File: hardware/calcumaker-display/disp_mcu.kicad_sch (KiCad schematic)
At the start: 8 parts, among them J3 SWD TC2030-NL, U4 STM32G031K8U6

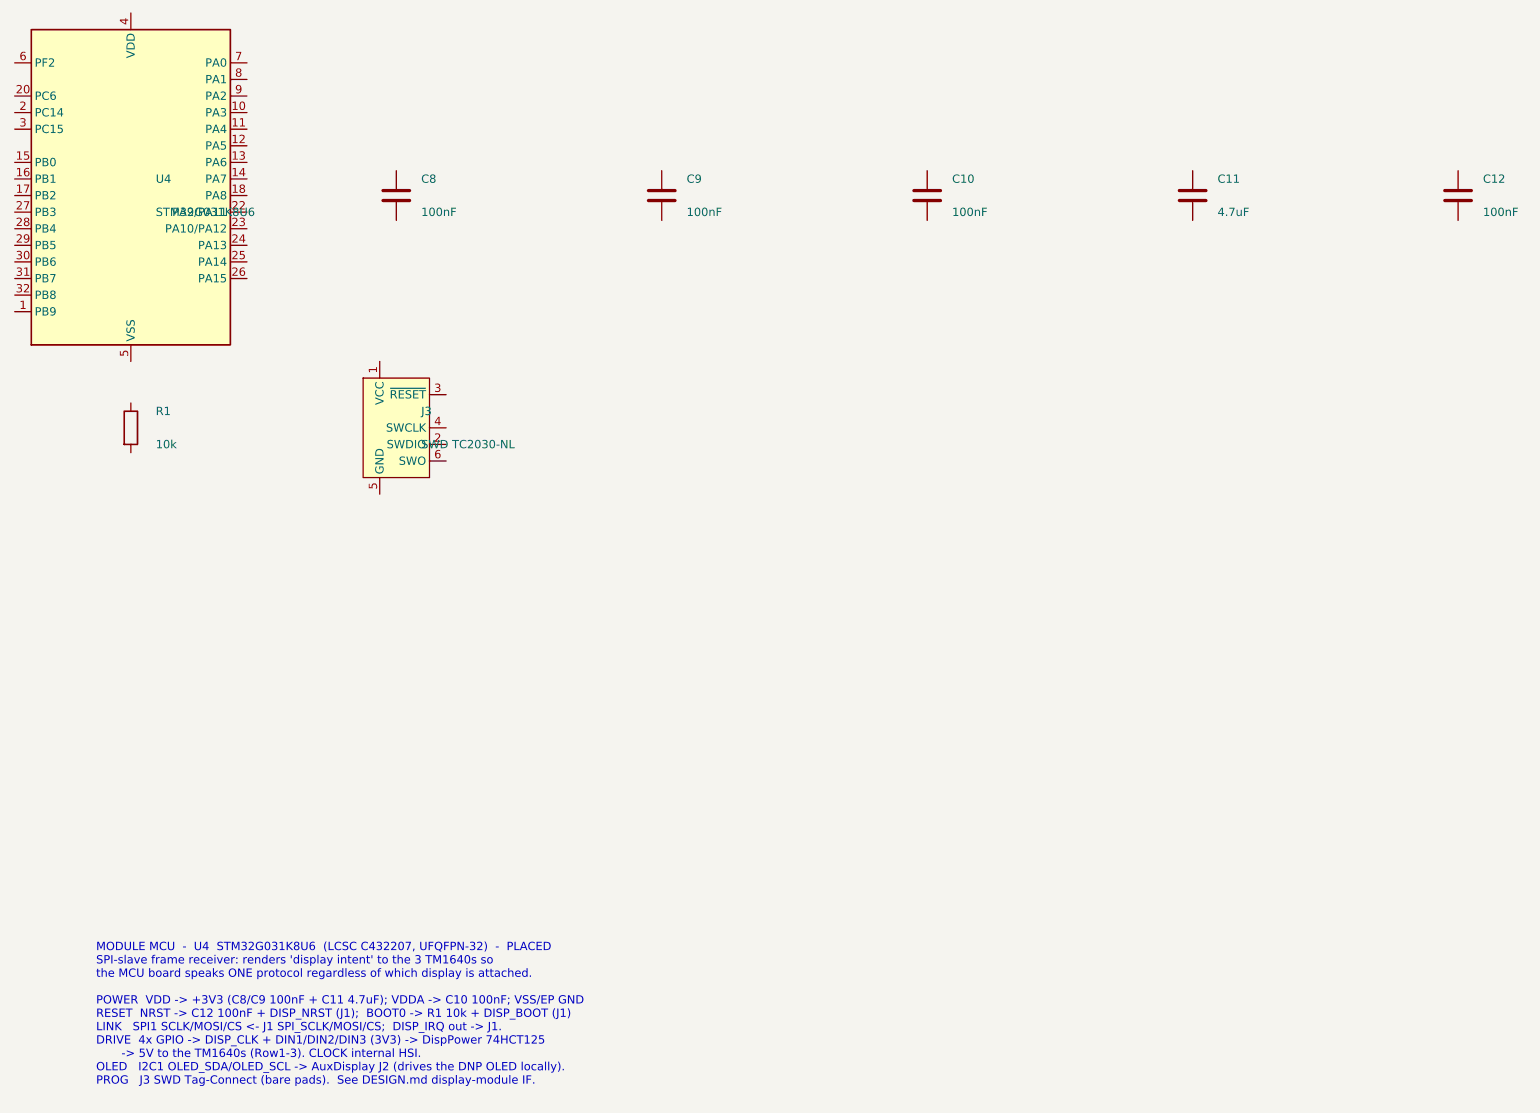
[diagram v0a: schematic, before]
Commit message: firmware: scaffold the two display-module targets + wire the module sheets
Firmware scaffold (all build; targets thumbv6m-none-eabi):
- calcumaker-display-proto: shared no_std wire protocol — the "display intent"
  DisplayFrame the U575 sends over SPI (text rows + flags + aux), with a
  fixed-length checksummed codec. Host-tested (cargo test: 3/3).
- calcumaker-display-fw: 7-seg module (STM32G031, embassy-stm32) — SPI-slave
  receiver + a bit-bang TM1640 driver + 7-seg render.
- calcumaker-matrix-fw: RGB-matrix module (RP2040, embassy-rp) — SPI-slave
  receiver + a 96x24 framebuffer/font blitter; WS2812 PIO output + SPI DMA
  stubbed as the bring-up TODOs.

Wire the one-off module schematic sheets (were placed-not-wired):
- kschgen: pin_geom now follows (extends ...) like pin_numbers, so derived
  symbols (STM32G031, 74xx) wire via net_pin.
- matrix rp2040 + rgb_power: RP2040 power/clock/flash/USB + the FET load switch
  and 3x single-gate level shifters are fully wired.
- display disp_mcu + disp_power: STM32G031 + the TPS61022 boost and 4x single-
  gate shifters are fully wired. (Quad 74xx buffers were multi-unit, which
  kschgen can't place fully, so the shifters are single-gate 74x1G125 — matching
  the keyboard's approach.)

All 4 boards check clean (mcu 46 / keyboard 179 / display 83 / matrix 2343, no
dup refs); wiring cut ERC pin_not_connected ~4x on both display modules.

Co-Authored-By: Claude Opus 4.8 (1M context) <noreply@anthropic.com>
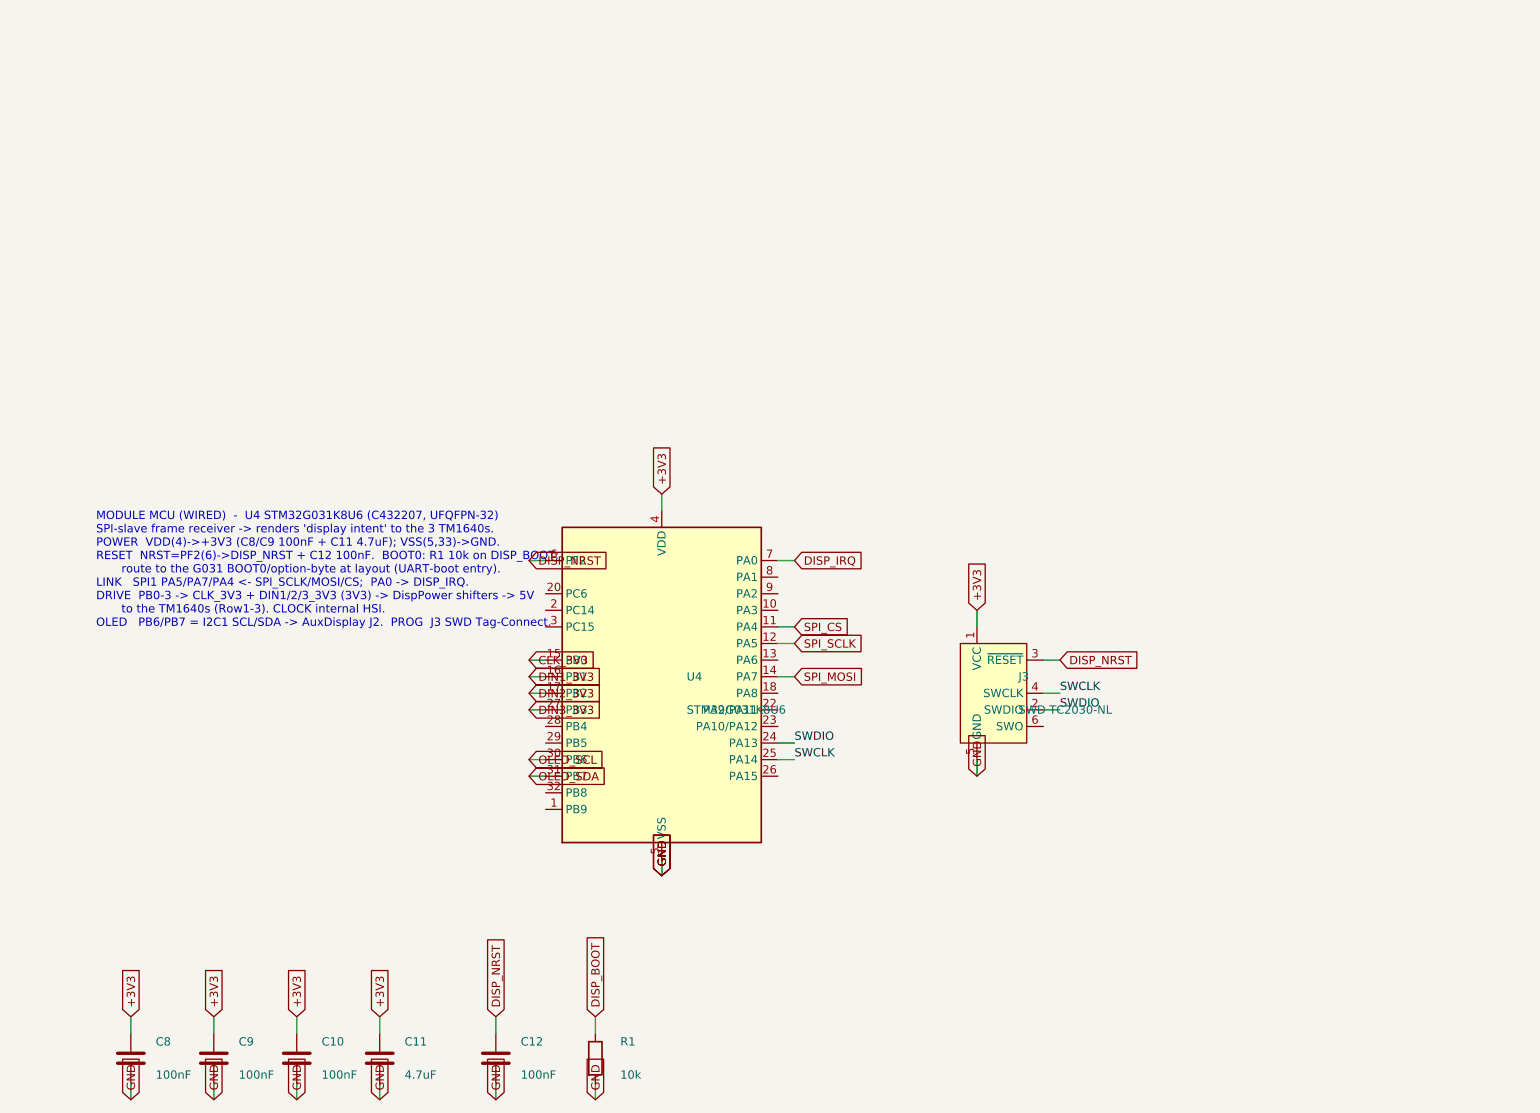
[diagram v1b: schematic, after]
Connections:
- net +3V3: now reaches C10.1
- net +3V3: now also C11.1, C8.1, C9.1, J3.1 (VCC), U4.4 (VDD)
- net GND: now reaches C10.2
- net GND: now also C11.2, C12.2, C8.2, C9.2, J3.5 (GND), R1.2, U4.33 (VSS), U4.5 (VSS)
- net DISP_BOOT: now reaches R1.1
- net SWDIO: now reaches J3.2 (SWDIO)
- net SWDIO: now also U4.24 (PA13)
- net DISP_NRST: now reaches J3.3 (~{RESET})
- net DISP_NRST: now also C12.1, U4.6 (PF2)
- net SWCLK: now reaches J3.4 (SWCLK)
- net SWCLK: now also U4.25 (PA14)
- net SPI_CS: now reaches U4.11 (PA4)
- net SPI_SCLK: now reaches U4.12 (PA5)
- net SPI_MOSI: now reaches U4.14 (PA7)
- net CLK_3V3: now reaches U4.15 (PB0)
- net DIN1_3V3: now reaches U4.16 (PB1)
- net DIN2_3V3: now reaches U4.17 (PB2)
- net DIN3_3V3: now reaches U4.27 (PB3)
- net OLED_SCL: now reaches U4.30 (PB6)
- net OLED_SDA: now reaches U4.31 (PB7)
- net DISP_IRQ: now reaches U4.7 (PA0)
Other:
- note added: "MODULE MCU (WIRED) - U4 STM32G031K8U6 (C432207, UFQFPN-32) SPI-slave frame receiver -> renders 'display intent' to the 3 TM1640s. POWER VDD(4)->+3V3 (C8/C9 100nF + C11 4.7uF); VSS(5,33)->GND. RESET NRST=PF2(6)->DISP_NRST + C12 100nF. BOOT0: R1 10k on DISP_BOOT; route to the G031 BOOT0/option-byte at layout (UART-boot entry). LINK SPI1 PA5/PA7/PA4 <- SPI_SCLK/MOSI/CS; PA0 -> DISP_IRQ. DRIVE PB0-3 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"
- note removed: "MODULE MCU - U4 STM32G031K8U6 (LCSC C432207, UFQFPN-32) - PLACED SPI-slave frame receiver: renders 'display intent' to the 3 TM1640s so the MCU board speaks ONE protocol regardless of which display is attached. POWER VDD -> +3V3 (C8/C9 100nF + C11 4.7uF); VDDA -> C10 100nF; VSS/EP GND RESET NRST -> C12 100nF + DISP_NRST (J1); BOOT0 -> R1 10k + DISP_BOOT (J1) LINK SPI1 SCLK/MOSI/CS <- J1 SPI_SCLK/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"
- title: Calcumaker 16 — Display — Module MCU (STM32G031K8U6, SPI-slave) -> Calcumaker 16 — Display — Module MCU (STM32G031K8U6, SPI-slave) — wired
